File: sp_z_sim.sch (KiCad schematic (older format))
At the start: 41 parts, among them J1 USB_B_Micro, J10 ADC_EXTRA, J11 IN+, J12 IN-, J13 CAL_3.3, J14 CAL_3.3, J15 FAN, J2 TEMP1, J3 TEMP1, J4 SWD, J5 Micro_SD_Card_Det, J6 OUT1, J7 OUT2, J8 4T_1, J9 4T_2, Q6 Q_NMOS_GSD

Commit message: almost done with bom. there are some issues
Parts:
- C1, C2, C3: OrderN (none) -> 490-10731-1-ND
- C28, C4: OrderN (none) -> 493-11829-1-ND
- C6: OrderN (none) -> 445-5207-1-ND
- D1: OrderN (none) -> 160-1446-1-ND
- D2: OrderN (none) -> SML-D12U1WT86CT-ND
- H1, H2, H3, J11, J12, J13, J14, J6, J7, J8, J9: OrderN (none) -> n/a
- J10: OrderN (none) -> 455-1706-ND
- J15, J2, J3: OrderN (none) -> 455-1704-ND
- J4: OrderN (none) -> 455-1708-ND
- Q6: OrderN SI2302CDS-T1-E3CT-ND -> BSS138-FDICT-ND
- R1, R10, R11, R2, R3, R4, R5, R6, R9: OrderN (none) -> 311-10.0KHRCT-ND
- R35, R36: OrderN (none) -> RC0603FR-0722RL
- R7, R8: OrderN (none) -> 311-1.00KHRCT-ND
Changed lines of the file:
@@
 F 2 "LED_SMD:LED_0603_1608Metric" V 4750 1450 50  0001 C CNN
 F 3 "~" V 4750 1450 50  0001 C CNN
+F 4 "160-1446-1-ND" H 4750 1450 50  0001 C CNN "OrderN"
 	1    4750 1450
 	-1   0    0    1
@@
 F 2 "LED_SMD:LED_0603_1608Metric" V 4750 1550 50  0001 C CNN
 F 3 "~" V 4750 1550 50  0001 C CNN
+F 4 "SML-D12U1WT86CT-ND" H 4750 1550 50  0001 C CNN "OrderN"
 	1    4750 1550
 	-1   0    0    1
@@
 F 2 "Resistor_SMD:R_0603_1608Metric" H 5200 1450 50  0001 C CNN
 F 3 "~" H 5200 1450 50  0001 C CNN
+F 4 " 311-1.00KHRCT-ND " H 5200 1450 50  0001 C CNN "OrderN"
 	1    5200 1450
 	0    1    1    0
@@
 F 2 "Resistor_SMD:R_0603_1608Metric" H 5200 1550 50  0001 C CNN
 F 3 "~" H 5200 1550 50  0001 C CNN
+F 4 " 311-1.00KHRCT-ND " H 5200 1550 50  0001 C CNN "OrderN"
 	1    5200 1550
 	0    1    1    0
@@
 F 2 "Connector_JST:JST_PH_B6B-PH-K_1x06_P2.00mm_Vertical" H 1950 1400 50  0001 C CNN
 F 3 "~" H 1950 1400 50  0001 C CNN
+F 4 "455-1708-ND" H 1950 1400 50  0001 C CNN "OrderN"
 	1    1950 1400
 	1    0    0    1
@@
 F 2 "Resistor_SMD:R_0603_1608Metric" H 2300 2500 50  0001 C CNN
 F 3 "~" H 2300 2500 50  0001 C CNN
+F 4 " 311-10.0KHRCT-ND" H 2300 2500 50  0001 C CNN "OrderN"
 	1    2300 2500
 	-1   0    0    1
@@
 F 2 "Connector_JST:JST_PH_B2B-PH-K_1x02_P2.00mm_Vertical" H 1900 2700 50  0001 C CNN
 F 3 "~" H 1900 2700 50  0001 C CNN
+F 4 "455-1704-ND" H 1900 2700 50  0001 C CNN "OrderN"
 	1    1900 2700
 	1    0    0    -1
@@
 F 2 "Capacitor_SMD:C_0603_1608Metric" H 2600 2550 50  0001 C CNN
 F 3 "~" H 2600 2550 50  0001 C CNN
+F 4 "490-10731-1-ND" H 2600 2550 50  0001 C CNN "OrderN"
 	1    2600 2550
 	1    0    0    -1
@@
 F 2 "Resistor_SMD:R_0603_1608Metric" H 2300 3500 50  0001 C CNN
 F 3 "~" H 2300 3500 50  0001 C CNN
+F 4 " 311-10.0KHRCT-ND" H 2300 3500 50  0001 C CNN "OrderN"
 	1    2300 3500
 	-1   0    0    1
@@
 F 2 "Capacitor_SMD:C_0603_1608Metric" H 2600 3550 50  0001 C CNN
 F 3 "~" H 2600 3550 50  0001 C CNN
+F 4 "490-10731-1-ND" H 2600 3550 50  0001 C CNN "OrderN"
 	1    2600 3550
 	1    0    0    -1
@@
 F 2 "Connector_JST:JST_PH_B2B-PH-K_1x02_P2.00mm_Vertical" H 1900 3700 50  0001 C CNN
 F 3 "~" H 1900 3700 50  0001 C CNN
+F 4 "455-1704-ND" H 1900 3700 50  0001 C CNN "OrderN"
 	1    1900 3700
 	1    0    0    -1
@@
 F 2 "TestPoint:TestPoint_Pad_4.0x4.0mm" H 6500 1950 50  0001 C CNN
 F 3 "~" H 6500 1950 50  0001 C CNN
+F 4 "n/a" H 6500 1950 50  0001 C CNN "OrderN"
 	1    6500 1950
 	-1   0    0    1
@@
 F 2 "TestPoint:TestPoint_Pad_4.0x4.0mm" H 6500 2350 50  0001 C CNN
 F 3 "~" H 6500 2350 50  0001 C CNN
+F 4 "n/a" H 6500 2350 50  0001 C CNN "OrderN"
 	1    6500 2350
 	-1   0    0    1
@@
 F 2 "TestPoint:TestPoint_Pad_4.0x4.0mm" H 6500 2450 50  0001 C CNN
 F 3 "~" H 6500 2450 50  0001 C CNN
+F 4 "n/a" H 6500 2450 50  0001 C CNN "OrderN"
 	1    6500 2450
 	-1   0    0    1
@@
 F 2 "TestPoint:TestPoint_Pad_4.0x4.0mm" H 6500 2050 50  0001 C CNN
 F 3 "~" H 6500 2050 50  0001 C CNN
+F 4 "n/a" H 6500 2050 50  0001 C CNN "OrderN"
 	1    6500 2050
 	-1   0    0    1
@@
 F 2 "Capacitor_SMD:C_0603_1608Metric" H 4650 5550 50  0001 C CNN
 F 3 "~" H 4650 5550 50  0001 C CNN
+F 4 "490-10731-1-ND" H 4650 5550 50  0001 C CNN "OrderN"
 	1    4650 5550
 	1    0    0    -1
@@
 F 2 "Resistor_SMD:R_0603_1608Metric" H 5400 4350 50  0001 C CNN
 F 3 "~" H 5400 4350 50  0001 C CNN
+F 4 " 311-10.0KHRCT-ND" H 5400 4350 50  0001 C CNN "OrderN"
 	1    5400 4350
 	-1   0    0    1
@@
 F 2 "Resistor_SMD:R_0603_1608Metric" H 5300 4350 50  0001 C CNN
 F 3 "~" H 5300 4350 50  0001 C CNN
+F 4 " 311-10.0KHRCT-ND" H 5300 4350 50  0001 C CNN "OrderN"
 	1    5300 4350
 	-1   0    0    1
@@
 F 2 "Resistor_SMD:R_0603_1608Metric" H 5200 4350 50  0001 C CNN
 F 3 "~" H 5200 4350 50  0001 C CNN
+F 4 " 311-10.0KHRCT-ND" H 5200 4350 50  0001 C CNN "OrderN"
 	1    5200 4350
 	-1   0    0    1
@@
 F 2 "Resistor_SMD:R_0603_1608Metric" H 5100 4350 50  0001 C CNN
 F 3 "~" H 5100 4350 50  0001 C CNN
+F 4 " 311-10.0KHRCT-ND" H 5100 4350 50  0001 C CNN "OrderN"
 	1    5100 4350
 	-1   0    0    1
@@
 F 2 "Resistor_SMD:R_0603_1608Metric" H 5000 4350 50  0001 C CNN
 F 3 "~" H 5000 4350 50  0001 C CNN
+F 4 " 311-10.0KHRCT-ND" H 5000 4350 50  0001 C CNN "OrderN"
 	1    5000 4350
 	-1   0    0    1
@@
 F 2 "Resistor_SMD:R_0603_1608Metric" H 4900 4350 50  0001 C CNN
 F 3 "~" H 4900 4350 50  0001 C CNN
+F 4 " 311-10.0KHRCT-ND" H 4900 4350 50  0001 C CNN "OrderN"
 	1    4900 4350
 	-1   0    0    1
@@
 F 2 "Resistor_SMD:R_0603_1608Metric" H 4800 4350 50  0001 C CNN
 F 3 "~" H 4800 4350 50  0001 C CNN
+F 4 " 311-10.0KHRCT-ND" H 4800 4350 50  0001 C CNN "OrderN"
 	1    4800 4350
 	-1   0    0    1
@@
 F 3 "~" H 9850 1700 50  0001 C CNN
 F 4 "https://www.digikey.se/product-detail/en/nichicon/URS1J101MPD1TD/493-11829-1-ND/4320229" H 9850 1700 50  0001 C CNN "digikey"
+F 5 "493-11829-1-ND" H 9850 1700 50  0001 C CNN "OrderN"
 	1    9850 1700
 	-1   0    0    -1
@@
 F 2 "Connector_JST:JST_PH_B4B-PH-K_1x04_P2.00mm_Vertical" H 1950 4650 50  0001 C CNN
 F 3 "~" H 1950 4650 50  0001 C CNN
+F 4 " 455-1706-ND " H 1950 4650 50  0001 C CNN "OrderN"
 	1    1950 4650
 	1    0    0    -1
@@
 F 2 "TestPoint:TestPoint_Pad_4.0x4.0mm" H 9000 1800 50  0001 C CNN
 F 3 "~" H 9000 1800 50  0001 C CNN
+F 4 "n/a" H 9000 1800 50  0001 C CNN "OrderN"
 	1    9000 1800
 	1    0    0    -1
@@
 F 2 "TestPoint:TestPoint_Pad_4.0x4.0mm" H 9000 1600 50  0001 C CNN
 F 3 "~" H 9000 1600 50  0001 C CNN
+F 4 "n/a" H 9000 1600 50  0001 C CNN "OrderN"
 	1    9000 1600
 	1    0    0    -1
@@
 F 2 "Capacitor_SMD:C_1206_3216Metric" H 9500 1700 50  0001 C CNN
 F 3 "~" H 9500 1700 50  0001 C CNN
+F 4 "445-5207-1-ND" H 9500 1700 50  0001 C CNN "OrderN"
 	1    9500 1700
 	-1   0    0    -1
@@
 F 2 "Resistor_SMD:R_0603_1608Metric" H 1800 1950 50  0001 C CNN
 F 3 "~" H 1800 1950 50  0001 C CNN
+F 4 "RC0603FR-0722RL" H 1800 1950 50  0001 C CNN "OrderN"
 	1    1800 1950
 	0    -1   -1   0
@@
 F 2 "Resistor_SMD:R_0603_1608Metric" H 1800 2050 50  0001 C CNN
 F 3 "~" H 1800 2050 50  0001 C CNN
+F 4 "RC0603FR-0722RL" H 1800 2050 50  0001 C CNN "OrderN"
 	1    1800 2050
 	0    -1   -1   0
@@
 F 2 "TestPoint:TestPoint_Pad_3.0x3.0mm" H 9350 4500 50  0001 C CNN
 F 3 "~" H 9350 4500 50  0001 C CNN
+F 4 "n/a" H 9350 4500 50  0001 C CNN "OrderN"
 	1    9350 4500
 	1    0    0    -1
@@
 F 2 "TestPoint:TestPoint_Pad_3.0x3.0mm" H 9350 4650 50  0001 C CNN
 F 3 "~" H 9350 4650 50  0001 C CNN
+F 4 "n/a" H 9350 4650 50  0001 C CNN "OrderN"
 	1    9350 4650
 	1    0    0    -1
@@
 F 2 "Package_TO_SOT_SMD:SOT-23" H 5350 6900 50  0001 C CNN
 F 3 "~" H 5150 6800 50  0001 C CNN
-F 4 "SI2302CDS-T1-E3CT-ND" H 5150 6800 50  0001 C CNN "OrderN"
+F 4 "BSS138-FDICT-ND" H 5150 6800 50  0001 C CNN "OrderN"
 	1    5150 6800
 	1    0    0    -1
@@
 F 2 "Connector_JST:JST_PH_B2B-PH-K_1x02_P2.00mm_Vertical" H 5850 6400 50  0001 C CNN
 F 3 "~" H 5850 6400 50  0001 C CNN
+F 4 "455-1704-ND" H 5850 6400 50  0001 C CNN "OrderN"
 	1    5850 6400
 	-1   0    0    1
@@
 F 2 "MountingHole:MountingHole_3.2mm_M3" H 9250 5550 50  0001 C CNN
 F 3 "~" H 9250 5550 50  0001 C CNN
+F 4 "n/a" H 9250 5550 50  0001 C CNN "OrderN"
 	1    9250 5550
 	1    0    0    -1
@@
 F 2 "MountingHole:MountingHole_3.2mm_M3" H 9250 5750 50  0001 C CNN
 F 3 "~" H 9250 5750 50  0001 C CNN
+F 4 "n/a" H 9250 5750 50  0001 C CNN "OrderN"
 	1    9250 5750
 	1    0    0    -1
@@
 F 2 "MountingHole:MountingHole_3.2mm_M3" H 9250 5950 50  0001 C CNN
 F 3 "~" H 9250 5950 50  0001 C CNN
+F 4 "n/a" H 9250 5950 50  0001 C CNN "OrderN"
 	1    9250 5950
 	1    0    0    -1
@@
 F 3 "~" H 10200 1700 50  0001 C CNN
 F 4 "https://www.digikey.se/product-detail/en/nichicon/URS1J101MPD1TD/493-11829-1-ND/4320229" H 10200 1700 50  0001 C CNN "digikey"
+F 5 "493-11829-1-ND" H 10200 1700 50  0001 C CNN "OrderN"
 	1    10200 1700
 	-1   0    0    -1

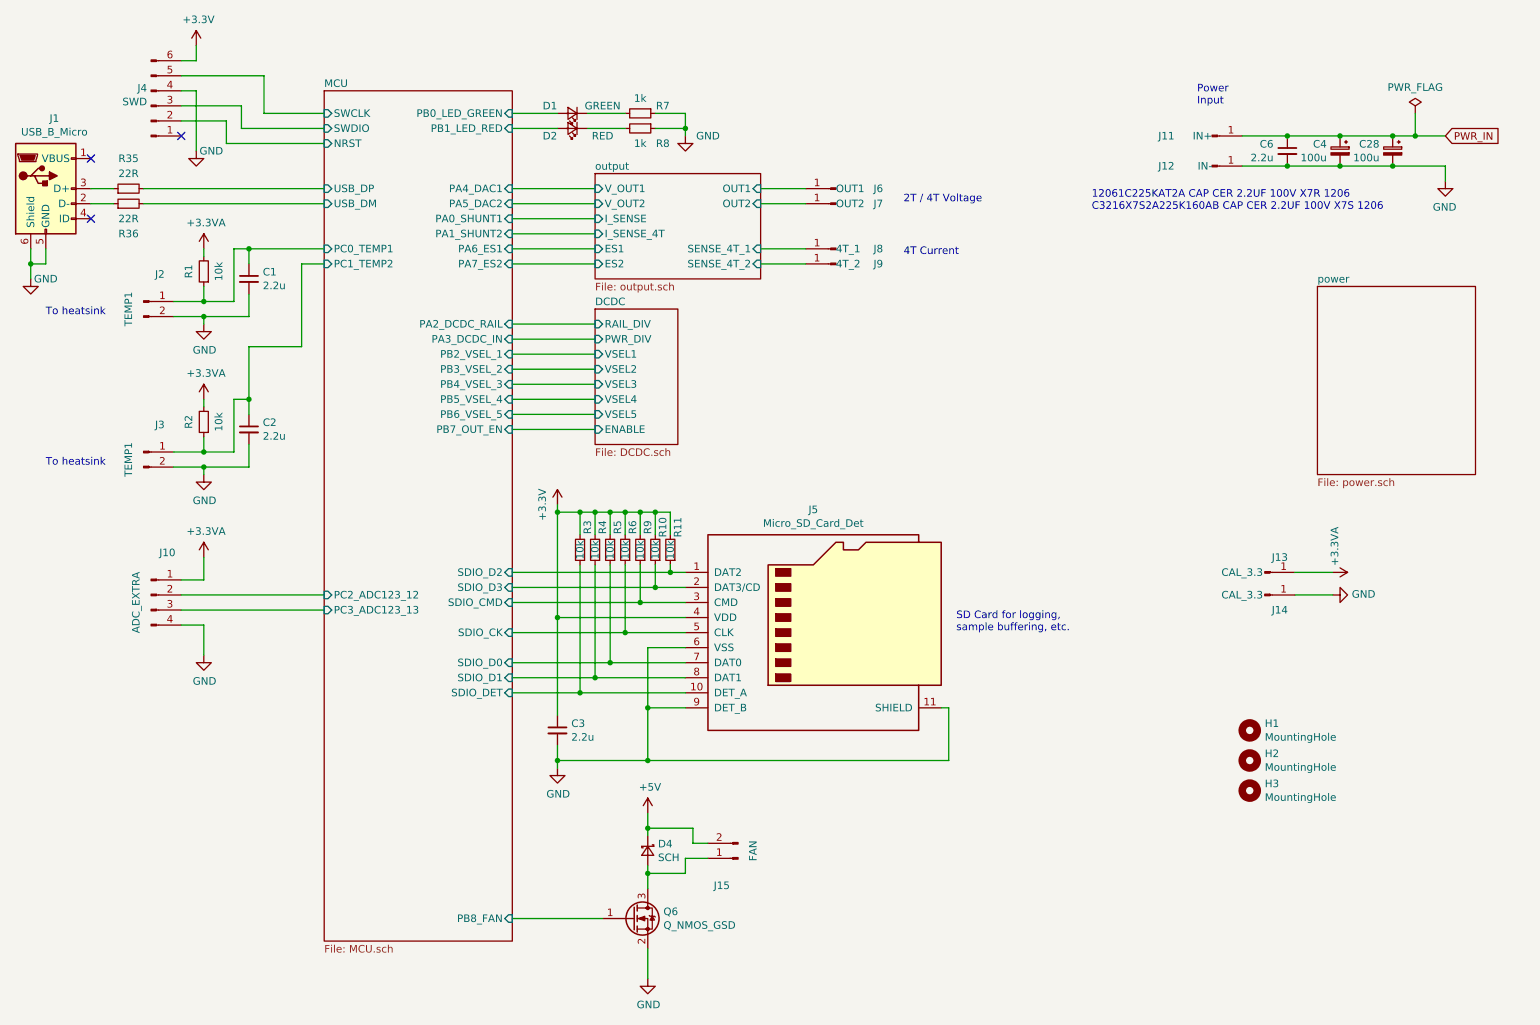
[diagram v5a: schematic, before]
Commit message: Added testpoints, changed connectors, changed shunts
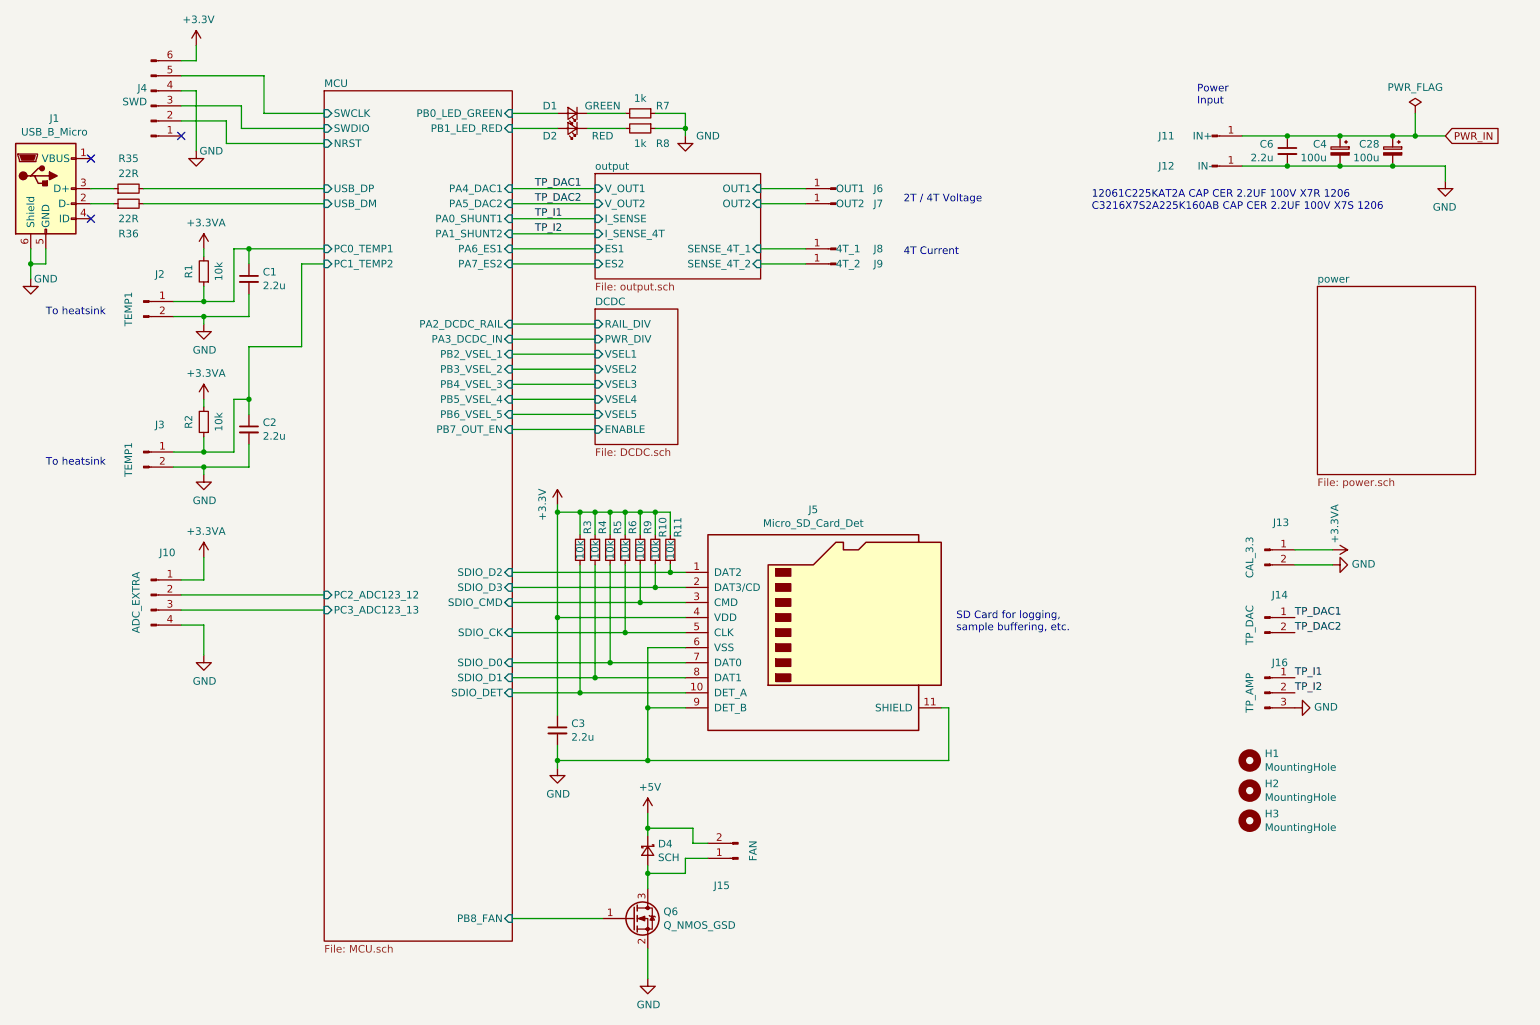
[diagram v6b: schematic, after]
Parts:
- removed J13, J14: CAL_3.3, TestPoint:TestPoint_Pad_3.0x3.0mm, symbol Connector:Conn_01x01_Male
- added J13: CAL_3.3, Connector_JST:JST_PH_B2B-PH-K_1x02_P2.00mm_Vertical, symbol Connector:Conn_01x02_Male
- added J14: TP_DAC, Connector_JST:JST_PH_B2B-PH-K_1x02_P2.00mm_Vertical, symbol Connector:Conn_01x02_Male
- added J16: TP_AMP, Connector_JST:JST_PH_B3B-PH-K_1x03_P2.00mm_Vertical, symbol Connector:Conn_01x03_Male
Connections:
- net +3.3VA: now also J13.1 (Pin_1)
- net GND: now also J13.2 (Pin_2), J16.3 (Pin_3)
- new net TP_DAC1: J14.1 (Pin_1)
- new net TP_DAC2: J14.2 (Pin_2)
- new net TP_I1: J16.1 (Pin_1)
- new net TP_I2: J16.2 (Pin_2)
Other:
- moved on the sheet: H1, H2, H3
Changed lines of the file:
@@
 L power:+3.3VA #PWR036
 U 1 1 5DB45B95
-P 9800 4500
-F 0 "#PWR036" H 9950 4500 50  0001 C CNN
-F 1 "+3.3VA" H 9627 4515 50  0000 C CNN
-F 2 "" H 9800 4500 50  0001 C CNN
-F 3 "" H 9800 4500 50  0001 C CNN
-	1    9800 4500
+P 9800 4350
+F 0 "#PWR036" H 9950 4350 50  0001 C CNN
+F 1 "+3.3VA" H 9627 4365 50  0000 C CNN
+F 2 "" H 9800 4350 50  0001 C CNN
+F 3 "" H 9800 4350 50  0001 C CNN
+	1    9800 4350
 	0    1    1    0
 $EndComp
@@
 L power:GND #PWR038
 U 1 1 5DB46A69
-P 9800 4650
-F 0 "#PWR038" H 9800 4400 50  0001 C CNN
-F 1 "GND" V 9805 4522 50  0000 R CNN
-F 2 "" H 9800 4650 50  0001 C CNN
-F 3 "" H 9800 4650 50  0001 C CNN
-	1    9800 4650
+P 9800 4450
+F 0 "#PWR038" H 9800 4200 50  0001 C CNN
+F 1 "GND" V 9805 4322 50  0000 R CNN
+F 2 "" H 9800 4450 50  0001 C CNN
+F 3 "" H 9800 4450 50  0001 C CNN
+	1    9800 4450
 	0    -1   -1   0
 $EndComp
-$Comp
-L Connector:Conn_01x01_Male J13
-U 1 1 5DB475B5
-P 9350 4500
-F 0 "J13" H 9450 4600 50  0000 C CNN
-F 1 "CAL_3.3" H 9200 4500 50  0000 C CNN
-F 2 "TestPoint:TestPoint_Pad_3.0x3.0mm" H 9350 4500 50  0001 C CNN
-F 3 "~" H 9350 4500 50  0001 C CNN
-F 4 "n/a" H 9350 4500 50  0001 C CNN "OrderN"
-	1    9350 4500
-	1    0    0    -1
-$EndComp
-$Comp
-L Connector:Conn_01x01_Male J14
-U 1 1 5DB47B33
-P 9350 4650
-F 0 "J14" H 9450 4550 50  0000 C CNN
-F 1 "CAL_3.3" H 9200 4650 50  0000 C CNN
-F 2 "TestPoint:TestPoint_Pad_3.0x3.0mm" H 9350 4650 50  0001 C CNN
-F 3 "~" H 9350 4650 50  0001 C CNN
-F 4 "n/a" H 9350 4650 50  0001 C CNN "OrderN"
-	1    9350 4650
-	1    0    0    -1
-$EndComp
-Wire Wire Line
-	9550 4500 9800 4500
-Wire Wire Line
-	9800 4650 9550 4650
+Wire Wire Line
+	9550 4350 9800 4350
+Wire Wire Line
+	9800 4450 9550 4450
 $Comp
 L Device:Q_NMOS_GSD Q6
@@
 L Mechanical:MountingHole H1
 U 1 1 5DB5F2C6
-P 9250 5550
-F 0 "H1" H 9350 5596 50  0000 L CNN
-F 1 "MountingHole" H 9350 5505 50  0000 L CNN
-F 2 "MountingHole:MountingHole_3.2mm_M3" H 9250 5550 50  0001 C CNN
-F 3 "~" H 9250 5550 50  0001 C CNN
-F 4 "n/a" H 9250 5550 50  0001 C CNN "OrderN"
-	1    9250 5550
-	1    0    0    -1
-$EndComp
-$Comp
-L Mechanical:MountingHole H2
-U 1 1 5DB60163
 P 9250 5750
-F 0 "H2" H 9350 5796 50  0000 L CNN
+F 0 "H1" H 9350 5796 50  0000 L CNN
 F 1 "MountingHole" H 9350 5705 50  0000 L CNN
 F 2 "MountingHole:MountingHole_3.2mm_M3" H 9250 5750 50  0001 C CNN
@@
 $EndComp
 $Comp
-L Mechanical:MountingHole H3
-U 1 1 5DB6057C
+L Mechanical:MountingHole H2
+U 1 1 5DB60163
 P 9250 5950
-F 0 "H3" H 9350 5996 50  0000 L CNN
+F 0 "H2" H 9350 5996 50  0000 L CNN
 F 1 "MountingHole" H 9350 5905 50  0000 L CNN
 F 2 "MountingHole:MountingHole_3.2mm_M3" H 9250 5950 50  0001 C CNN
@@
 F 4 "n/a" H 9250 5950 50  0001 C CNN "OrderN"
 	1    9250 5950
+	1    0    0    -1
+$EndComp
+$Comp
+L Mechanical:MountingHole H3
+U 1 1 5DB6057C
+P 9250 6150
+F 0 "H3" H 9350 6196 50  0000 L CNN
+F 1 "MountingHole" H 9350 6105 50  0000 L CNN
+F 2 "MountingHole:MountingHole_3.2mm_M3" H 9250 6150 50  0001 C CNN
+F 3 "~" H 9250 6150 50  0001 C CNN
+F 4 "n/a" H 9250 6150 50  0001 C CNN "OrderN"
+	1    9250 6150
 	1    0    0    -1
 $EndComp
@@
 Wire Wire Line
 	10200 1800 9850 1800
+Text Label 4500 1950 0    50   ~ 0
+TP_DAC1
+Text Label 4500 2050 0    50   ~ 0
+TP_DAC2
+Text Label 9550 4900 0    50   ~ 0
+TP_DAC2
+Text Label 9550 4800 0    50   ~ 0
+TP_DAC1
+$Comp
+L Connector:Conn_01x02_Male J13
+U 1 1 5DC55E05
+P 9350 4350
+F 0 "J13" H 9458 4531 50  0000 C CNN
+F 1 "CAL_3.3" V 9250 4300 50  0000 C CNN
+F 2 "Connector_JST:JST_PH_B2B-PH-K_1x02_P2.00mm_Vertical" H 9350 4350 50  0001 C CNN
+F 3 "~" H 9350 4350 50  0001 C CNN
+F 4 "455-1704-ND" H 9350 4350 50  0001 C CNN "OrderN"
+	1    9350 4350
+	1    0    0    -1
+$EndComp
+$Comp
+L Connector:Conn_01x02_Male J14
+U 1 1 5DC57413
+P 9350 4800
+F 0 "J14" H 9450 4950 50  0000 C CNN
+F 1 "TP_DAC" V 9250 4750 50  0000 C CNN
+F 2 "Connector_JST:JST_PH_B2B-PH-K_1x02_P2.00mm_Vertical" H 9350 4800 50  0001 C CNN
+F 3 "~" H 9350 4800 50  0001 C CNN
+F 4 "455-1704-ND" H 9350 4800 50  0001 C CNN "OrderN"
+	1    9350 4800
+	1    0    0    -1
+$EndComp
+Text Label 4500 2150 0    50   ~ 0
+TP_I1
+Text Label 4500 2250 0    50   ~ 0
+TP_I2
+Text Label 9550 5200 0    50   ~ 0
+TP_I1
+Text Label 9550 5300 0    50   ~ 0
+TP_I2
+$Comp
+L Connector:Conn_01x03_Male J16
+U 1 1 5DC72E50
+P 9350 5300
+F 0 "J16" H 9450 5500 50  0000 C CNN
+F 1 "TP_AMP" V 9250 5300 50  0000 C CNN
+F 2 "Connector_JST:JST_PH_B3B-PH-K_1x03_P2.00mm_Vertical" H 9350 5300 50  0001 C CNN
+F 3 "~" H 9350 5300 50  0001 C CNN
+	1    9350 5300
+	1    0    0    -1
+$EndComp
+$Comp
+L power:GND #PWR?
+U 1 1 5DC40DCD
+P 9550 5400
+F 0 "#PWR?" H 9550 5150 50  0001 C CNN
+F 1 "GND" V 9555 5272 50  0000 R CNN
+F 2 "" H 9550 5400 50  0001 C CNN
+F 3 "" H 9550 5400 50  0001 C CNN
+	1    9550 5400
+	0    -1   -1   0
+$EndComp
 $EndSCHEMATC

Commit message: all components now have an OrderN in the matrix
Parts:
- J1: OrderN (none) -> WM1399CT-ND
- J16: OrderN (none) -> 455-1705-ND
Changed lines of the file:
@@
 F 2 "Connector_USB:USB_Micro-B_Molex-105017-0001" H 1400 1900 50  0001 C CNN
 F 3 "~" H 1400 1900 50  0001 C CNN
+F 4 " WM1399CT-ND " H 1250 1950 50  0001 C CNN "OrderN"
 	1    1250 1950
 	1    0    0    -1
@@
 F 2 "Connector_JST:JST_PH_B3B-PH-K_1x03_P2.00mm_Vertical" H 9350 5300 50  0001 C CNN
 F 3 "~" H 9350 5300 50  0001 C CNN
+F 4 " 455-1705-ND " H 9350 5300 50  0001 C CNN "OrderN"
 	1    9350 5300
 	1    0    0    -1

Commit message: Changed fan mosfet part number
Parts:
- Q6: OrderN BSS138-FDICT-ND -> NTR3C21NZT1GOSCT-ND
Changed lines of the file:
@@
 F 2 "Package_TO_SOT_SMD:SOT-23" H 5350 6900 50  0001 C CNN
 F 3 "~" H 5150 6800 50  0001 C CNN
-F 4 "BSS138-FDICT-ND" H 5150 6800 50  0001 C CNN "OrderN"
+F 4 "NTR3C21NZT1GOSCT-ND" H 5150 6800 50  0001 C CNN "OrderN"
 	1    5150 6800
 	1    0    0    -1
